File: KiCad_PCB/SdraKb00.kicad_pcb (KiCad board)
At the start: 2 copper layers, 85.3 x 83.4 mm, 77 parts, among them J1 AVR-ISP-6, SW00 SW_Push_45deg, SW01 SW_Push_45deg, SW02 SW_Push_45deg, SW03 RotaryEncoder_Switch, SW10 SW_Push_45deg, SW11 SW_Push_45deg, SW12 SW_Push_45deg, SW13 SW_Push_45deg, SW20 SW_Push_45deg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

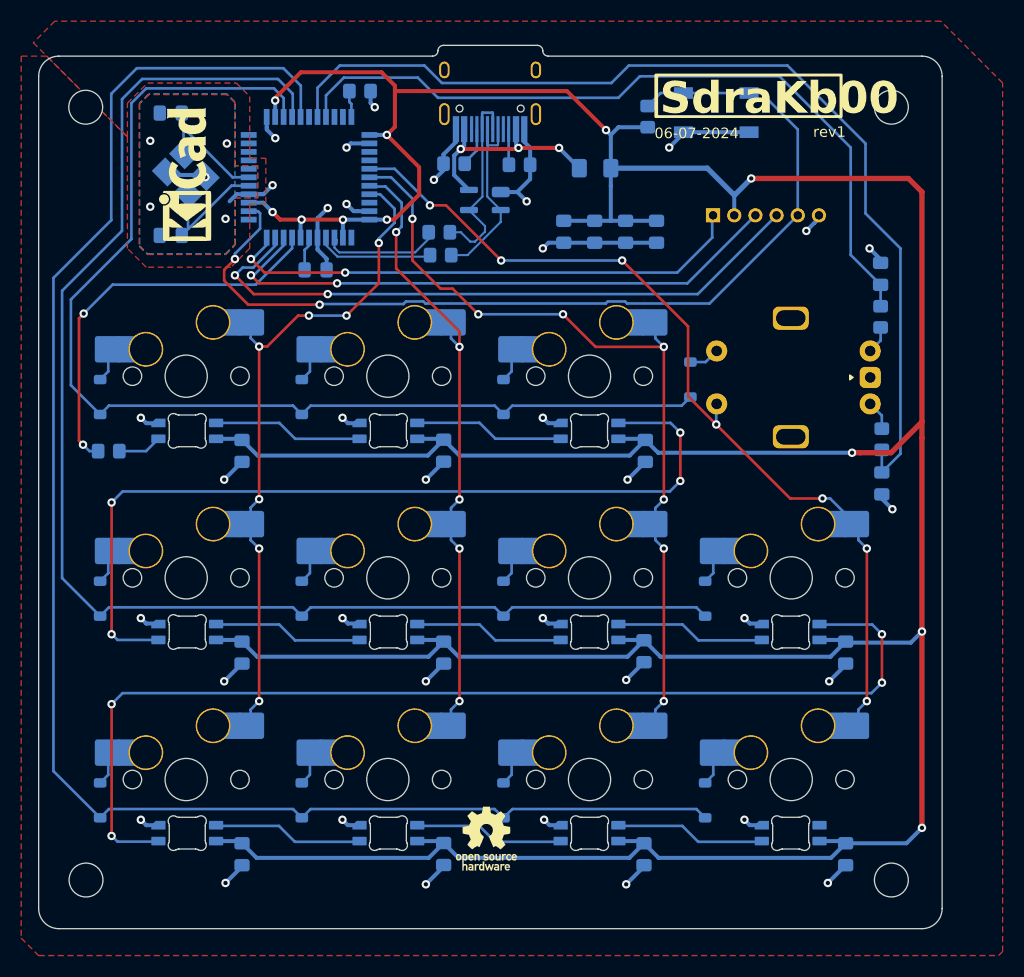
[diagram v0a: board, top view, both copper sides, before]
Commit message: Adding power indicator LED.
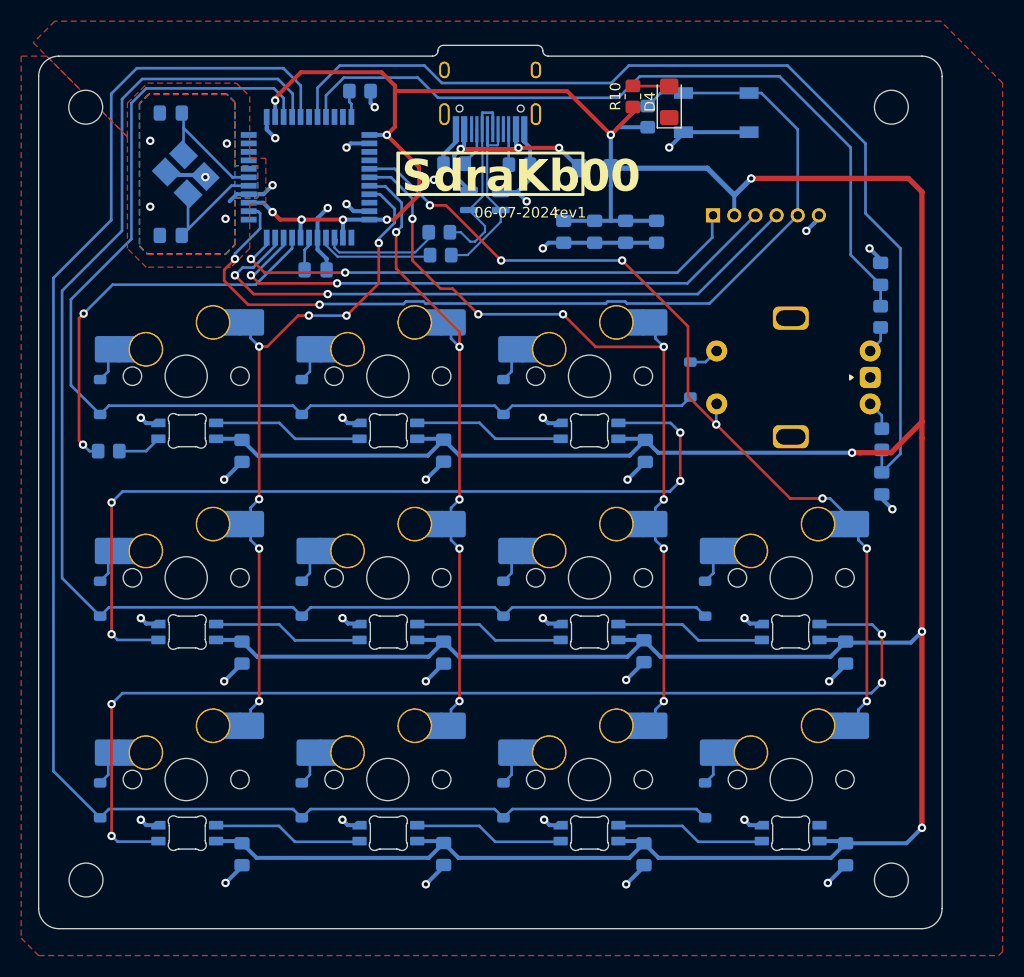
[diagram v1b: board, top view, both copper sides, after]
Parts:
- removed REF**: KiCad-Logo_5mm_SilkScreen, Symbol:KiCad-Logo_5mm_SilkScreen
- removed REF**: OSHW-Logo_5.7x6mm_SilkScreen, Symbol:OSHW-Logo_5.7x6mm_SilkScreen
- added D4: RED 1.8V, LED_SMD:LED_1206_3216Metric_Pad1.42x1.75mm_HandSolder, F.Cu at (160.7, 67.1)
- added R10: 640, Resistor_SMD:R_0805_2012Metric_Pad1.20x1.40mm_HandSolder, F.Cu at (157.2, 66.5)
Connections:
- U1 pad 36: unconnected-(U1-PF7-Pad36) -> STATUS_LED
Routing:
- net +5V: track 418.6 -> 422.1 mm
- net Net-(D4-A): track 0.00 -> 3.44 mm

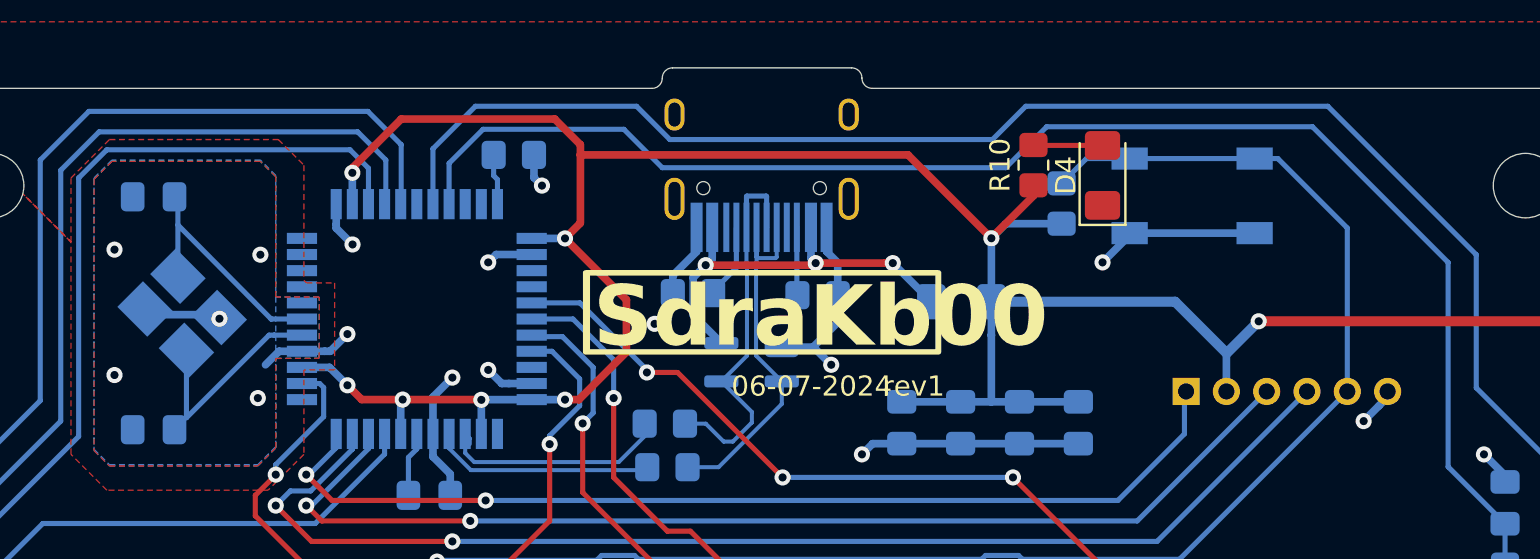
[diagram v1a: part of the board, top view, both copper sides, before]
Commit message: Re-placing silkscreen.
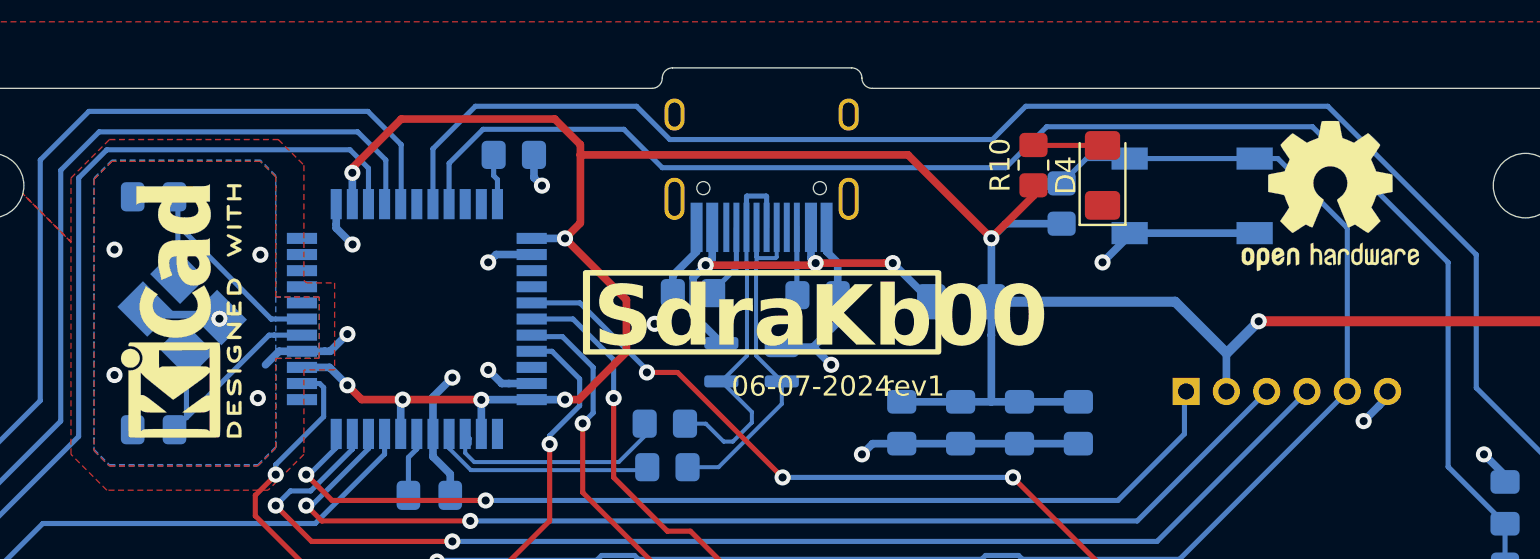
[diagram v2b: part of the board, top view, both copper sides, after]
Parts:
- added REF**: KiCad-Logo2_5mm_SilkScreen, Symbol:KiCad-Logo2_5mm_SilkScreen, F.Cu at (114.9, 73.8)
- added REF**: OSHW-Logo2_9.8x8mm_SilkScreen, Symbol:OSHW-Logo2_9.8x8mm_SilkScreen, F.Cu at (172.0, 68.1)
